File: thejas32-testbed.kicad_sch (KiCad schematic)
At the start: 98 parts, among them J1 Conn_02x04_Odd_Even, J10 Conn_02x10_Odd_Even, J11 Conn_02x03_Odd_Even, J12 Conn_02x20_Odd_Even, J13 Conn_02x06_Odd_Even, J2 USB_B_Micro, J3 Conn_02x03_Odd_Even, J4 Conn_02x04_Odd_Even, J6 Conn_02x06_Odd_Even, J7 Conn_01x05, U1 Pico Master, U2 THEJAS32, U3 Pico Slave, U6 W25Q16JVSSIQ

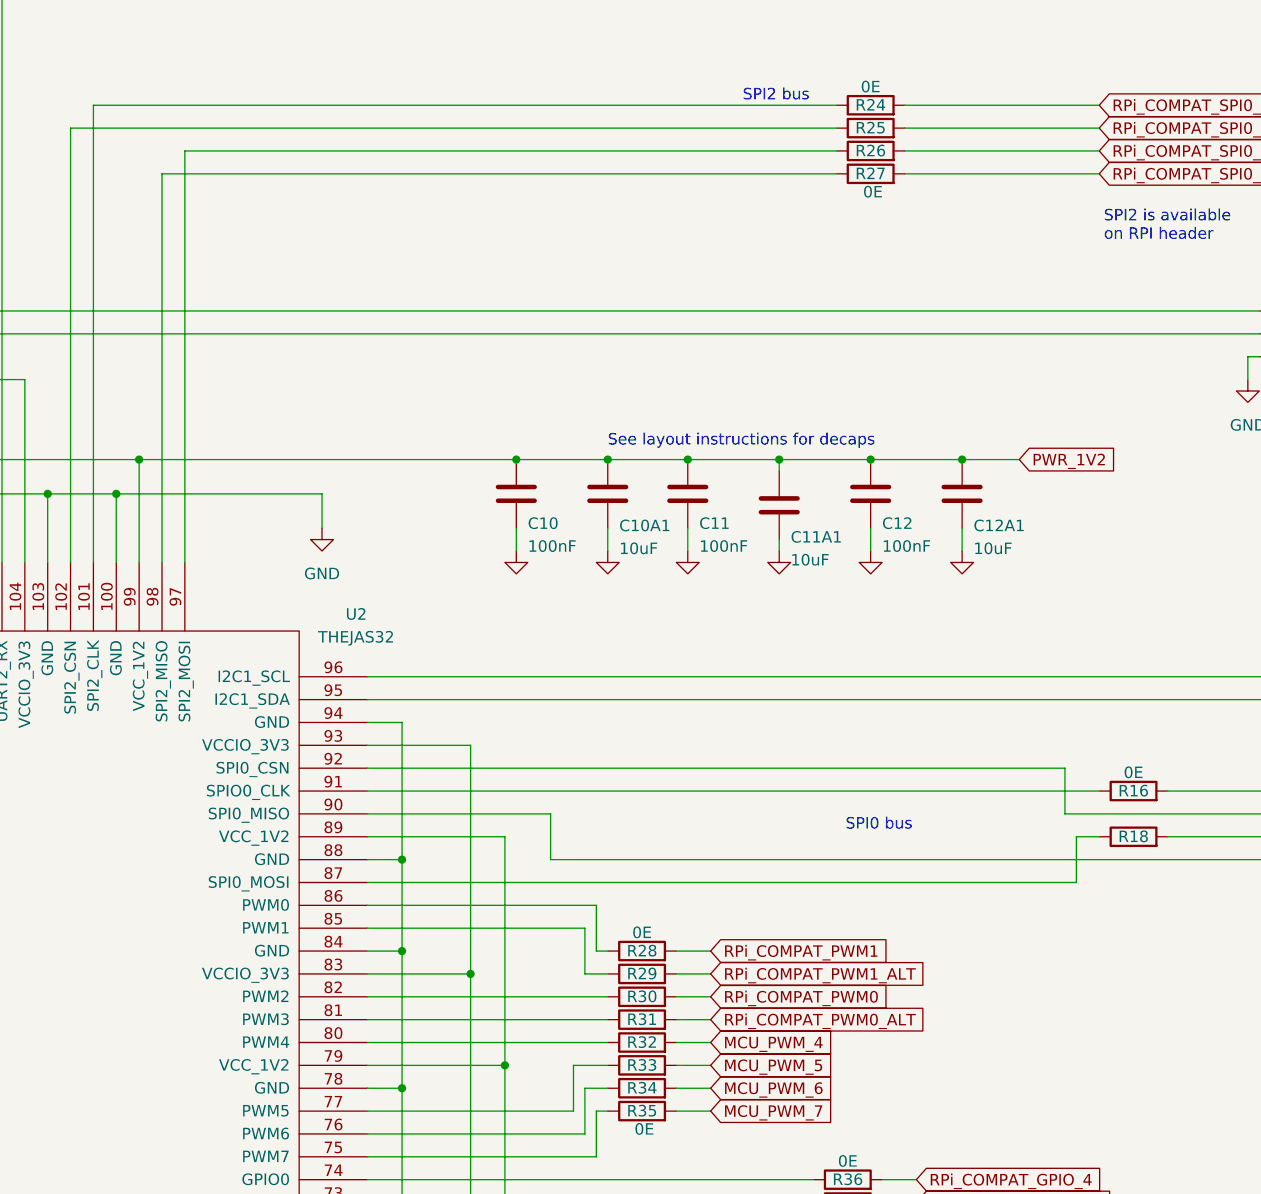
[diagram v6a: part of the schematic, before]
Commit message: Minor schematic changes
Mounting holes are M3 pads.
PWM pin routed to Pico is excluded from header
Position of connectors improved.
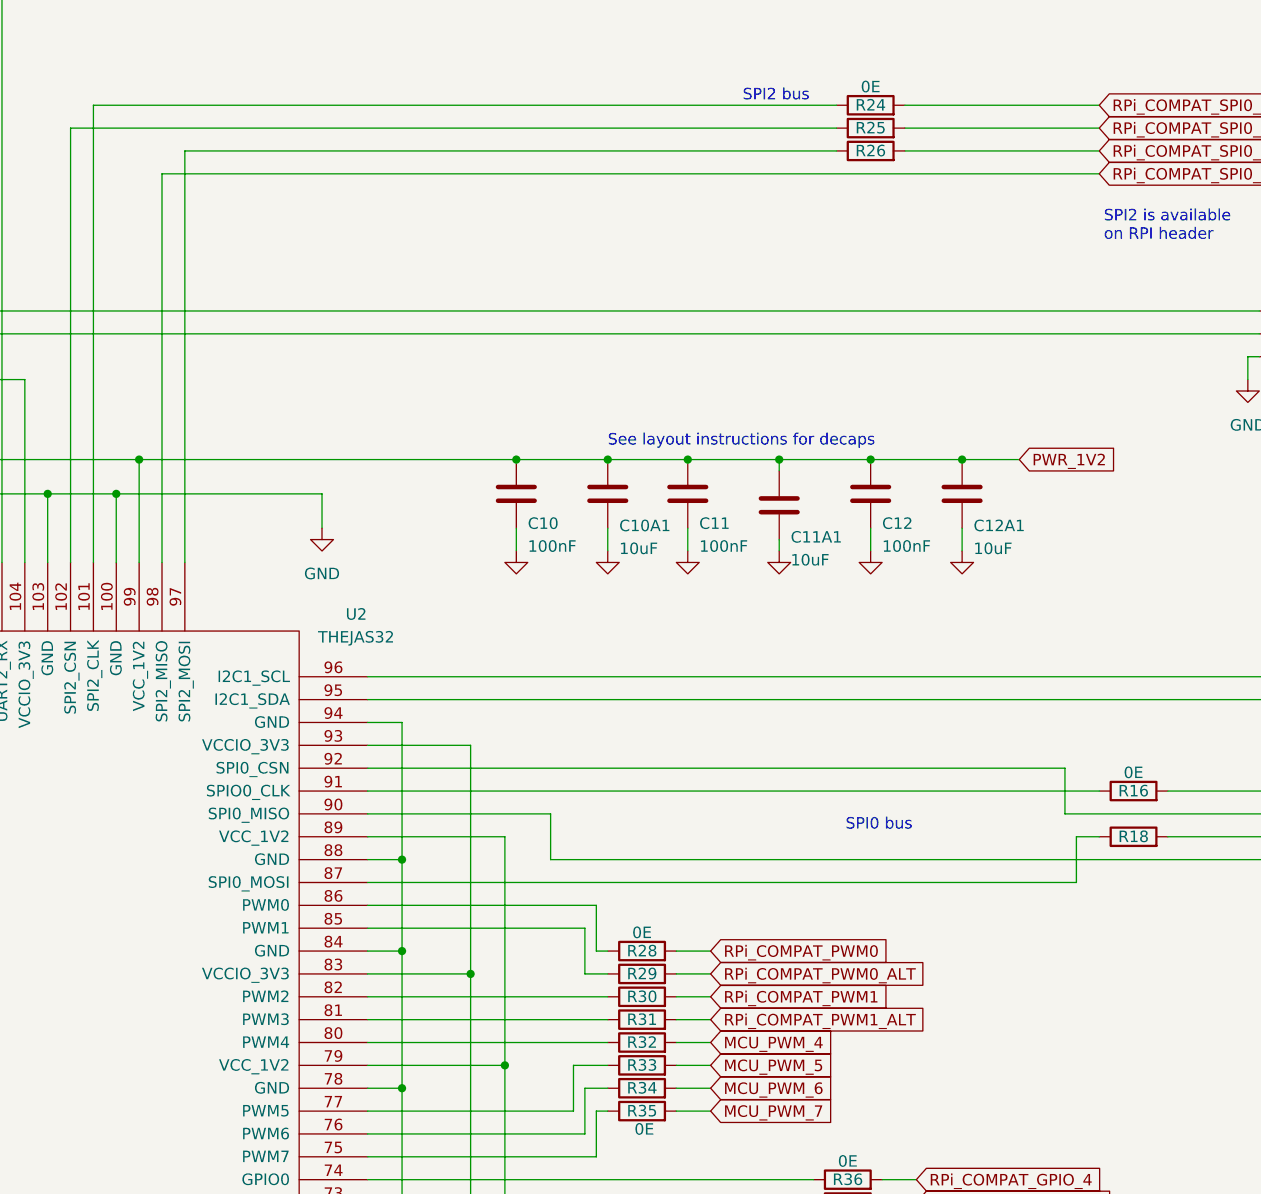
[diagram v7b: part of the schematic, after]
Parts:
- removed R27: 0E, project_lib:proj_R_0603_1608Metric_Pad0.98x0.95mm_HandSolder, symbol Project-Specific:R_HandSolderable
- TP1, TP2, TP3: footprint MountingHole:MountingHole_3.2mm_M3_Pad -> MountingHole:MountingHole_3mm_Pad_TopBottom
- TP4, TP5, TP6: footprint MountingHole:MountingHole_3.2mm_M3_Pad -> MountingHole:MountingHole_3.2mm_M3_Pad_TopBottom
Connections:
- net RPi_COMPAT_PWM0: now also R28.2; no longer R30.2
- net RPi_COMPAT_PWM0_ALT: now also R29.2; no longer R31.2
- net RPi_COMPAT_PWM1: now also R30.2; no longer R28.2
- net RPi_COMPAT_PWM1_ALT: now also R31.2; no longer R29.2
- net RPi_COMPAT_SPI0_MISO: now also U2.98 (SPI2_MISO)
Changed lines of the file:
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@@
 	(wire
 		(pts
-			(xy 350.52 198.12) (xy 328.93 198.12)
-		)
-		(stroke
-			(width 0)
-			(type default)
-		)
-	)
-	(wire
-		(pts
 			(xy 307.34 360.68) (xy 307.34 340.36)
 		)
@@
 	(wire
 		(pts
-			(xy 246.38 198.12) (xy 321.31 198.12)
+			(xy 246.38 198.12) (xy 350.52 198.12)
 		)
 		(stroke
@@
 	(global_label "RPi_COMPAT_PWM1"
 		(shape input)
-		(at 307.34 284.48 0)
+		(at 307.34 289.56 0)
 		(fields_autoplaced yes)
 		(effects
@@
 		)
 		(property "Intersheetrefs" "${INTERSHEET_REFS}"
-			(at 328.1656 284.48 0)
+			(at 328.1656 289.56 0)
 			(effects
 				(font
@@
 	(global_label "RPi_COMPAT_PWM0_ALT"
 		(shape input)
-		(at 307.34 292.1 0)
+		(at 307.34 287.02 0)
 		(fields_autoplaced yes)
 		(effects
@@
 		)
 		(property "Intersheetrefs" "${INTERSHEET_REFS}"
-			(at 332.2175 292.1 0)
+			(at 332.2175 287.02 0)
 			(effects
 				(font
@@
 	(global_label "RPi_COMPAT_PWM0"
 		(shape input)
-		(at 307.34 289.56 0)
+		(at 307.34 284.48 0)
 		(fields_autoplaced yes)
 		(effects
@@
 		)
 		(property "Intersheetrefs" "${INTERSHEET_REFS}"
-			(at 328.1656 289.56 0)
+			(at 328.1656 284.48 0)
 			(effects
 				(font
@@
 	(global_label "RPi_COMPAT_PWM1_ALT"
 		(shape input)
-		(at 307.34 287.02 0)
+		(at 307.34 292.1 0)
 		(fields_autoplaced yes)
 		(effects
@@
 		)
 		(property "Intersheetrefs" "${INTERSHEET_REFS}"
-			(at 332.2175 287.02 0)
+			(at 332.2175 292.1 0)
 			(effects
 				(font
@@
 			)
 		)
-		(property "Footprint" "MountingHole:MountingHole_3.2mm_M3_Pad"
+		(property "Footprint" "MountingHole:MountingHole_3.2mm_M3_Pad_TopBottom"
 			(at 759.46 372.11 0)
 			(effects
@@
 			)
 		)
-		(property "Footprint" "MountingHole:MountingHole_3.2mm_M3_Pad"
+		(property "Footprint" "MountingHole:MountingHole_3mm_Pad_TopBottom"
 			(at 745.49 372.11 0)
 			(effects
@@
 			)
 		)
-		(property "Footprint" "MountingHole:MountingHole_3.2mm_M3_Pad"
+		(property "Footprint" "MountingHole:MountingHole_3.2mm_M3_Pad_TopBottom"
 			(at 772.16 372.11 0)
 			(effects
@@
 			)
 		)
-		(property "Footprint" "MountingHole:MountingHole_3.2mm_M3_Pad"
+		(property "Footprint" "MountingHole:MountingHole_3.2mm_M3_Pad_TopBottom"
 			(at 765.7385 371.9382 0)
 			(effects
@@
 			)
 		)
-		(property "Footprint" "MountingHole:MountingHole_3.2mm_M3_Pad"
+		(property "Footprint" "MountingHole:MountingHole_3mm_Pad_TopBottom"
 			(at 737.87 372.11 0)
 			(effects
@@
 	)
 	(symbol
-		(lib_id "Project-Specific:R_HandSolderable")
-		(at 325.12 198.12 90)
-		(unit 1)
-		(exclude_from_sim no)
-		(in_bom yes)
-		(on_board yes)
-		(dnp no)
-		(property "Reference" "R27"
-			(at 325.12 198.12 90)
-			(effects
-				(font
-					(size 1.27 1.27)
-				)
-			)
-		)
-		(property "Value" "0E"
-			(at 325.374 200.152 90)
-			(effects
-				(font
-					(size 1.27 1.27)
-				)
-			)
-		)
-		(property "Footprint" "project_lib:proj_R_0603_1608Metric_Pad0.98x0.95mm_HandSolder"
-			(at 325.12 199.898 90)
-			(effects
-				(font
-					(size 1.27 1.27)
-				)
-				(hide yes)
-			)
-		)
-		(property "Datasheet" "~"
-			(at 325.12 198.12 0)
-			(effects
-				(font
-					(size 1.27 1.27)
-				)
-				(hide yes)
-			)
-		)
-		(property "Description" "Resistor"
-			(at 325.12 198.12 0)
-			(effects
-				(font
-					(size 1.27 1.27)
-				)
-				(hide yes)
-			)
-		)
-		(pin "2"
-		)
-		(pin "1"
-		)
-		(instances
-			(project "thejas32-testbed"
-				(path "/012bf1cf-e3e3-4b01-8e23-6b37d758d0e3"
-					(reference "R27")
-					(unit 1)
-				)
-			)
-		)
-	)
-	(symbol
 		(lib_id "Project-Specific:DCAP_Near")
 		(at 331.47 375.92 0)
@@
 			)
 		)
-		(property "Footprint" "MountingHole:MountingHole_3.2mm_M3_Pad"
+		(property "Footprint" "MountingHole:MountingHole_3mm_Pad_TopBottom"
 			(at 753.11 372.11 0)
 			(effects

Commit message: Single pico, new layout
Figured two picos was too much as a concept. So, simplify.

Reduce number of jumpers etc also (especially in passthrough).

The single pico breaks out pins conveniently for users for
usage.
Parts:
- removed J1, J4: Conn_02x04_Odd_Even, Connector_PinHeader_2.54mm:PinHeader_2x04_P2.54mm_Vertical, symbol Connector_Generic:Conn_02x04_Odd_Even
- removed J11: Conn_02x03_Odd_Even, Connector_PinHeader_2.54mm:PinHeader_2x03_P2.54mm_Vertical, symbol Connector_Generic:Conn_02x03_Odd_Even
- removed J13, J6: Conn_02x06_Odd_Even, Connector_PinHeader_2.54mm:PinHeader_2x06_P2.54mm_Vertical, symbol Connector_Generic:Conn_02x06_Odd_Even
- removed R3: 10K, project_lib:proj_R_0603_1608Metric_Pad0.98x0.95mm_HandSolder, symbol Project-Specific:R_HandSolderable
- removed TP3: Mounting Hole, MountingHole:MountingHole_3mm_Pad_TopBottom, symbol Connector:TestPoint
- removed TP5: Mounting Hole, MountingHole:MountingHole_3.2mm_M3_Pad_TopBottom, symbol Connector:TestPoint
- removed U3: Pico Slave, RPi_Pico:RPi_Pico_SMD_TH, symbol MCU_RaspberryPi_and_Boards:Pico
- added H1, H2, H3, H4, H5: MountingHole, MountingHole:MountingHole_3mm, symbol Mechanical:MountingHole
- added J1: Conn_01x04, Connector_PinHeader_2.54mm:PinHeader_1x04_P2.54mm_Vertical, symbol Connector_Generic:Conn_01x04
- added J11, J13, J8: Conn_01x03, Connector_PinHeader_2.54mm:PinHeader_1x03_P2.54mm_Vertical, symbol Connector_Generic:Conn_01x03
- added J4: Conn_02x05_Odd_Even, Connector_PinHeader_2.54mm:PinHeader_2x05_P2.54mm_Vertical, symbol Connector_Generic:Conn_02x05_Odd_Even
- added J6: Conn_01x10, Connector_PinHeader_2.54mm:PinHeader_1x10_P2.54mm_Vertical, symbol Connector_Generic:Conn_01x10
- added J9: Conn_01x05, Connector_PinHeader_2.54mm:PinHeader_1x05_P2.54mm_Vertical, symbol Connector_Generic:Conn_01x05
- added TP7: TestPoint, TestPoint:TestPoint_Pad_1.0x1.0mm, symbol Connector:TestPoint
- TP2: footprint MountingHole:MountingHole_3mm_Pad_TopBottom -> MountingHole:MountingHole_3.2mm_M3_Pad_TopBottom
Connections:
- net PICO_SLAVE_RUN is gone; now on net MCU_SPI1_MOSI: U1.21 (GPIO16)
- net GND: now also J1.1 (Pin_1), J11.3 (Pin_3), J13.3 (Pin_3), J4.10 (Pin_10), J4.9 (Pin_9), J6.10 (Pin_10), J6.5 (Pin_5), J8.3 (Pin_3), J9.3 (Pin_3)
- net MCU_GPIO_16: now also U1.4 (GPIO2); no longer J10.4 (Pin_4)
- net MCU_GPIO_18: now also J10.4 (Pin_4); no longer J10.6 (Pin_6)
- net MCU_GPIO_20: now also J10.6 (Pin_6); no longer J10.8 (Pin_8)
- net MCU_GPIO_22: now also J10.8 (Pin_8); no longer J10.10 (Pin_10)
- net MCU_GPIO_24: now also J10.10 (Pin_10); no longer J10.12 (Pin_12)
- net MCU_GPIO_26: now also J10.12 (Pin_12); no longer J10.14 (Pin_14)
- net MCU_GPIO_28: now also J10.14 (Pin_14); no longer J10.16 (Pin_16)
- net MCU_GPIO_30: now also J10.16 (Pin_16); no longer J10.18 (Pin_18)
- net MCU_I2C0_SCL: now also R4.2, U1.32 (GPIO27_ADC1), U2.33 (I2C0_SCL), J13.1 (Pin_1); no longer U1.9 (GPIO6)
- net MCU_I2C0_SDA: now also R5.2, U1.31 (GPIO26_ADC0), U2.34 (I2C0_SDA), J13.2 (Pin_2); no longer U1.10 (GPIO7)
- net MCU_I2C1_SCL: now also R6.2, U2.96 (I2C1_SCL), J4.6 (Pin_6)
- net MCU_I2C1_SDA: now also R7.2, U2.95 (I2C1_SDA), J4.8 (Pin_8)
- net MCU_PWM_7: now also U1.19 (GPIO14); no longer U1.22 (GPIO17)
- net MCU_SPI0_CSN: now also U2.92 (SPI0_CSN), J4.3 (Pin_3)
- net MCU_SPI0_MISO: now also U2.90 (SPI0_MISO), J4.7 (Pin_7)
- net MCU_SPI0_MOSI: now also R18.2, J4.5 (Pin_5)
- net MCU_SPI0_SCK: now also R16.2, J4.1 (Pin_1)
- net MCU_SPI1_CSN: now also U1.22 (GPIO17), U2.39 (SPI1_SS), J9.4 (Pin_4); no longer U1.17 (GPIO13)
- net MCU_SPI1_MISO: now also U1.25 (GPIO19), U2.41 (SPI1_MISO), J9.1 (Pin_1); no longer U1.15 (GPIO11)
- net MCU_SPI1_MOSI: now also R22.2, J9.5 (Pin_5); no longer U1.16 (GPIO12)
- net MCU_SPI1_SCK: now also R20.2, U1.24 (GPIO18), J9.2 (Pin_2); no longer U1.14 (GPIO10)
- net PWR_3V3: now also J4.2 (Pin_2), J4.4 (Pin_4)
- net PWR_5V: now also JP4.2 (B); no longer J2.1 (VBUS), JP4.1 (A)
- net RPi_COMPAT_GPIO_4: now also U2.109 (GPIO31); no longer R36.2
- net at U2.45 (UART1_TX): now also J11.1 (Pin_1)
- net at U2.50 (UART1_RX): now also J11.2 (Pin_2)
- net at U1.1 (GPIO0): now also J8.1 (Pin_1)
- net at U1.2 (GPIO1): now also J8.2 (Pin_2)
- net at U1.29 (GPIO22): now also J1.3 (Pin_3)
- net at U1.30 (RUN): now also J1.4 (Pin_4)
- net at U1.34 (GPIO28_ADC2): now also J1.2 (Pin_2)
- net MCU_GPIO_00: now reaches U1.5 (GPIO3)
- net MCU_GPIO_00: now also R36.2
- net MCU_GPIO_31: no longer names the net of J10.17 (Pin_17)
- net MCU_GPIO_31: no longer U2.109 (GPIO31)
- net MCU_HEART_BEAT: no longer names the net of U2.16 (PROC_HEART_BEAT)
- net MCU_HEART_BEAT: now also TP7.1; no longer U1.24 (GPIO18)
- net PICO_COMM_1: no longer names the net of U1.11 (GPIO8)
- net PICO_COMM_1: now also J6.3 (Pin_3)
- net PICO_COMM_2: no longer names the net of U1.12 (GPIO9)
- net PICO_COMM_2: now also J6.4 (Pin_4)
- new net: J6.1 (Pin_1), U1.9 (GPIO6)
- new net: J6.2 (Pin_2), U1.10 (GPIO7)
- new net: J6.6 (Pin_6), U1.14 (GPIO10)
- new net: J6.7 (Pin_7), U1.15 (GPIO11)
- new net: J6.8 (Pin_8), U1.16 (GPIO12)
- new net: J6.9 (Pin_9), U1.17 (GPIO13)
- new net: J2.1 (VBUS), JP4.1 (A)
- no-connect marks 50 -> 16
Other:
- note added: "A Raspberry Pi Pico is used as the test bed driver. The Pico controls the entire system. User logic can run in both the THEJAS32 and the Pico."
- note added: "Combined I2C and SPI header"
- note added: "Non-plated mounting holes"
- note added: "Plated through holes"
- note added: "These test points are not real test points. They represent through holes on the board."
- note removed: "2x Raspberry Pi Picos are used as the test bed drivers. Master controls the entire system. Slave can help with some testing."
- note removed: "I2C0 is available on RPI header"
- note removed: "I2C1 can be tapped here. Short to send to RP2040"
- note removed: "Order of Pins: GND, CLK, CSN, MOSI, MISO VCC"
- note removed: "Order of Pins: VCC, CLK, CSN, MOSI, MISO GND"
- note removed: "Populate this to get power from main connector. Has benefits, including powering RP2040 for USB host."
- note removed: "Pull-down ensures Pico Slave doesn't run by default."
- note removed: "These test points are not real test points. They represent plated through holes on the edge of the board."
- note removed: "To communicate with slave Pico"
- note removed: "spi1 slave interface"
- moved on the sheet: J2, TP4, TP6
